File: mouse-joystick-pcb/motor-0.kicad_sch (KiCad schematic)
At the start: 28 parts, among them J1 Conn_01x04_P3.5mm_TBH_Horizon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, J2 Conn_01x02_P3.5mm_TBH_Horizon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, J3 Conn_01x05_P3.5mm_TBH_Horizon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, U1 TMC5130A-TA, U2 MAX6816, U5 Logic_LevelTranslator_LSF0102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, X1 16MHz_3.3V

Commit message: Adjust schmatic
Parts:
- removed C1, C2, C4, C5, C8, C9: 0.1uF_100V, Janelia:C_0402_1005Metric, symbol Janelia:C_0.1uF_100V_0402
- removed C10, C11: 2.2uF_100V, Janelia:C_0805_2012Metric, symbol Janelia:C_2.2uF_100V_0805
- removed C12, C13: 100uF_50V, Janelia:CAP_EEEHAH101UAP, symbol Janelia:CP_100uF_50V_8x10.2mm
- removed C3: 22nF_100V, Janelia:C_0603_1608Metric, symbol Janelia:C_22nF_100V_0603
- removed C6: 0.47uF_35V, Janelia:C_0402_1005Metric, symbol Janelia:C_0.47uF_35V_0402
- removed C7: 47uF_10V, Janelia:C_0805_2012Metric, symbol Janelia:C_47uF_10V_0805
- removed J1: Conn_01x04_P3.5mm_TBH_Horizontal_Screw, Janelia:PhoenixContact_MC_1,5_4-G-3.5_1x04_P3.50mm_Horizontal_Screw, symbol Janelia:Conn_01x04_P3.5mm_TBH_Horizontal_Screw
- removed J2: Conn_01x02_P3.5mm_TBH_Horizontal_Screw, Janelia:PhoenixContact_MC_1,5_2-G-3.5_1x02_P3.50mm_Horizontal_Screw, symbol Janelia:Conn_01x02_P3.5mm_TBH_Horizontal_Screw
- removed R5: 10, Janelia:R_0402_1005Metric, symbol Janelia:R_10_62.5mW_0402
- removed U1: TMC5130A-TA, Janelia:TQFP-48-1EP_7x7mm_P0.5mm_EP5x5mm_ThermalVias, symbol Janelia:TMC5130A-TA
- removed U2: MAX6816, Janelia:SOT192P237X122-4N, symbol Janelia:MAX6816
- removed X1: 16MHz_3.3V, Janelia:OSC_ECS-2520S33-160-FN-TR, symbol Janelia:Oscillator_16MHz_3.3V
- added C501, C502, C504, C505, C509, C510: 0.1uF_100V, Janelia:C_0402_1005Metric, symbol Janelia:C_0.1uF_100V_0402
- added C503: 22nF_100V, Janelia:C_0603_1608Metric, symbol Janelia:C_22nF_100V_0603
- added C506: 0.47uF_35V, Janelia:C_0402_1005Metric, symbol Janelia:C_0.47uF_35V_0402
- added C507: 47uF_10V, Janelia:C_0805_2012Metric, symbol Janelia:C_47uF_10V_0805
- added C512, C513: 2.2uF_100V, Janelia:C_0805_2012Metric, symbol Janelia:C_2.2uF_100V_0805
- added C514, C515: 100uF_50V, Janelia:CAP_EEEHAH101UAP, symbol Janelia:CP_100uF_50V_8x10.2mm
- added J501: Conn_01x02_P3.5mm_TBH_Horizontal_Screw, Janelia:PhoenixContact_MC_1,5_2-G-3.5_1x02_P3.50mm_Horizontal_Screw, symbol Janelia:Conn_01x02_P3.5mm_TBH_Horizontal_Screw
- added J502: Conn_01x04_P3.5mm_TBH_Horizontal_Screw, Janelia:PhoenixContact_MC_1,5_4-G-3.5_1x04_P3.50mm_Horizontal_Screw, symbol Janelia:Conn_01x04_P3.5mm_TBH_Horizontal_Screw
- added R503: 10, Janelia:R_0402_1005Metric, symbol Janelia:R_10_62.5mW_0402
- added U501: MAX6816, Janelia:SOT192P237X122-4N, symbol Janelia:MAX6816
- added U502: TMC5130A-TA, Janelia:TQFP-48-1EP_7x7mm_P0.5mm_EP5x5mm_ThermalVias, symbol Janelia:TMC5130A-TA
- added X501: 16MHz_3.3V, Janelia:OSC_ECS-2520S33-160-FN-TR, symbol Janelia:Oscillator_16MHz_3.3V
- renumbered C23 to C508, C25 to C511, C26 to C516, C24 to C517, J3 to J503, R1 to R501, R2 to R502, R9 to R504, U5 to U503
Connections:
- net +3.3V: now also C501.1, C502.1, C505.1, U501.4 (Vcc), U502.10 (VCC_IO), U502.12 (SPI_MODE), X501.4 (VDD)
- net +5V: now also C506.1, R503.1, U502.34 (VCC), U502.39 (VSA)
- net 5VOUT: now also C507.1, R503.2, U502.33 (5VOUT)
- net BMA1: now also J502.4 (Pin_4), U502.46 (OA1)
- net BMA2: now also J502.3 (Pin_3), U502.42 (OA2)
- net BMB1: now also J502.2 (Pin_2), U502.15 (OB1)
- net BMB2: now also J502.1 (Pin_1), U502.19 (OB2)
- net BRA: now also U502.44 (BRA)
- net BRB: now also U502.17 (BRB)
- net CIPO: now also U502.7 (SDO_NAO_CFG0)
- net CLOCK: now also U502.2 (CLK), X501.3 (OUT)
- net COPI: now also U502.5 (SDI_NAI_CFG1)
- net CPI: now also C503.2, U502.37 (CPI)
- net CPO: now also C503.1, U502.35 (CP0)
- net ENABLE: now also U502.29 (~{DRV_EN}_CFG6)
- net ENC_A_LS: now also U502.25 (ENCA_DCIN_CFG5)
- net ENC_B_LS: now also U502.24 (ENCB_DCEN_CFG4)
- net GND: now also C501.2, C502.2, C505.2, C506.2, C507.2, C509.2, C510.2, C512.2, C513.2, C514.2, C515.2, J501.1 (Pin_1), U501.1 (GND), U502.1 (TST_MODE), U502.11 (SD_MODE), U502.13 (GNDP), U502.23 (ENCN_DCO), U502.30 (AIN_IREF), U502.31 (NC), U502.32 (GNDA), U502.36 (NC), U502.48 (GNDP), U502.49 (EP), U502.6 (NC), U502.9 (REFR_DIR), X501.2 (GND)
- net REFL: now also J501.2 (Pin_2), U501.2 (IN)
- net REFL_DEBOUNCED: now also U501.3 (OUT), U502.8 (REFL_STEP)
- net SCK: now also U502.4 (SCK_CFG2)
- net VCP: now also C504.2, U502.38 (VCP)
- net VM: now also C504.1, C509.1, C510.1, C512.1, C513.1, C514.1, C515.1, U502.21 (VS), U502.40 (VS)
- net ~{CS}: now also U502.3 (~{CS}_CFG3)

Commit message: Finish v1.0 schematic
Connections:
- net ENABLE is gone; now on net GND: U502.29 (~{DRV_EN}_CFG6)
- net DIAG0: now reaches U502.26 (SWN_DIAG0)
- net +3.3V renamed VIO
- no-connect marks 5 -> 4
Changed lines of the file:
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@@
   (title_block
     (title "mouse-joystick-pcb")
-    (date "2024-10-07")
+    (date "2024-10-08")
     (rev "1.0")
     (company "Peter Polidoro")
@@
   (no_connect (at 270.51 139.7))
   (no_connect (at 85.09 44.45))
-  (no_connect (at 36.83 121.92))
   (no_connect (at 36.83 124.46))
   (no_connect (at 36.83 127))
@@
     (stroke (width 0) (type default))
   )
+  (wire (pts (xy 36.83 121.92) (xy 34.29 121.92))
+    (stroke (width 0) (type default))
+  )
   (wire (pts (xy 36.83 134.62) (xy 34.29 134.62))
     (stroke (width 0) (type default))
@@
     (effects (font (size 1.27 1.27)) (justify left bottom))
   )
+  (label "GND" (at 34.29 116.84 180) (fields_autoplaced)
+    (effects (font (size 1.27 1.27)) (justify right bottom))
+  )
   (label "VM" (at 135.89 36.83 90) (fields_autoplaced)
     (effects (font (size 1.27 1.27)) (justify left bottom))
@@
     (effects (font (size 1.27 1.27)) (justify left bottom))
   )
-  (hierarchical_label "+3.3V" (shape passive) (at 53.34 39.37 180) (fields_autoplaced)
+  (hierarchical_label "VIO" (shape passive) (at 53.34 39.37 180) (fields_autoplaced)
     (effects (font (size 1.27 1.27)) (justify right))
   )
@@
     (effects (font (size 1.27 1.27)) (justify right))
   )
-  (hierarchical_label "ENABLE" (shape input) (at 34.29 116.84 180) (fields_autoplaced)
-    (effects (font (size 1.27 1.27)) (justify right))
-  )
   (hierarchical_label "CIPO" (shape output) (at 34.29 93.98 180) (fields_autoplaced)
     (effects (font (size 1.27 1.27)) (justify right))
   )
+  (hierarchical_label "DIAG0" (shape output) (at 34.29 121.92 180) (fields_autoplaced)
+    (effects (font (size 1.27 1.27)) (justify right))
+  )

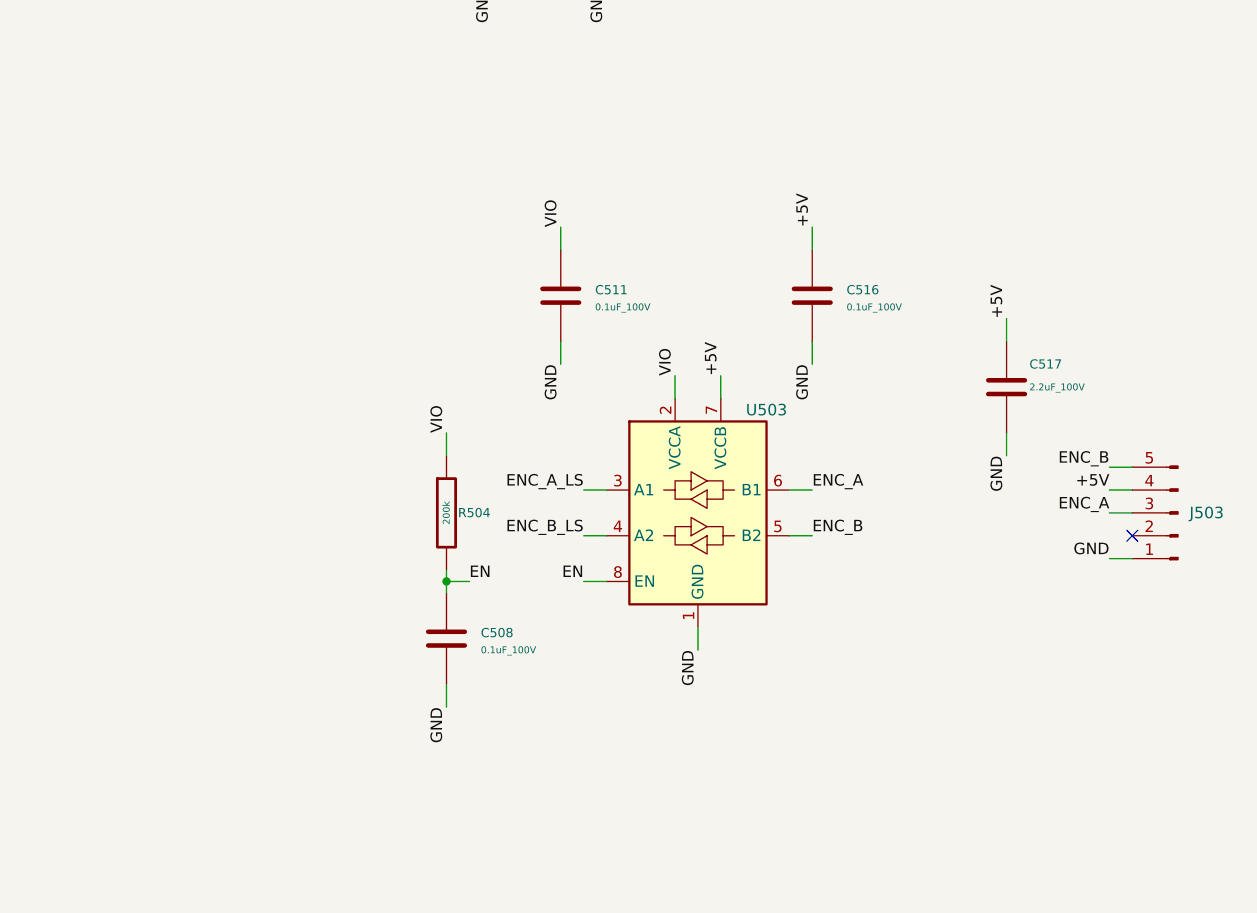
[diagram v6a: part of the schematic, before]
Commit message: Change encoder connector
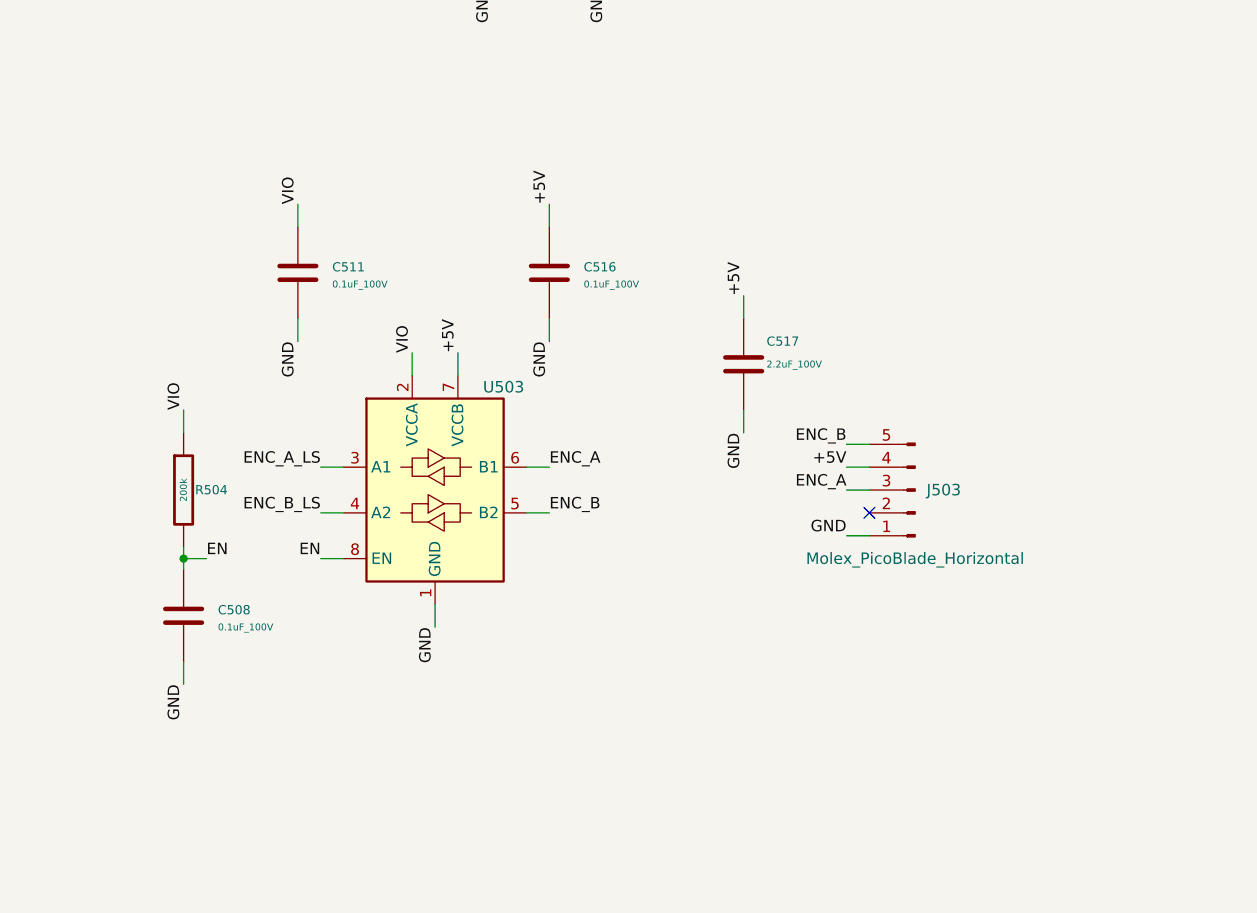
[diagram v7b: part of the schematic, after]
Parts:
- removed J503: Conn_01x05_P3.5mm_TBH_Horizontal_Screw, Janelia:PhoenixContact_MC_1,5_5-G-3.5_1x05_P3.50mm_Horizontal_Screw, symbol Janelia:Conn_01x05_P3.5mm_TBH_Horizontal_Screw
- added J503: Molex_PicoBlade_Horizontal, Janelia:MOLEX_0532610571, symbol Janelia:Conn_01x05_P1.25mm_Molex_PicoBlade_Horizontal
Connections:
- net +5V: now also J503.4 (Pin_4)
- net ENC_A: now also J503.3 (Pin_3)
- net ENC_B: now also J503.5 (Pin_5)
- net GND: now also J503.1 (Pin_1)
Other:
- moved on the sheet: C508, C511, C516, C517, R504, U503

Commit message: Finish routing
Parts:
- added R505: 1.8k, Janelia:R_0402_1005Metric, symbol Janelia:R_1.8k_0402
- C507: LCSC C2182652 -> C6119904; Manufacturer TDK Corporation -> HRE; Manufacturer Part Number C2012X5R1A476M125AC -> CGA0805X5R476M100MT; Vendor Digi-Key -> JLCPCB; Vendor Part Number 445-8239-1-ND -> C6119904
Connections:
- net VIO: now also R505.1
- net ~{CS}: now also R505.2
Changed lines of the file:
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@@
   (title_block
     (title "mouse-joystick-pcb")
-    (date "2024-10-15")
+    (date "2024-10-23")
     (rev "1.0")
     (company "Peter Polidoro")
@@
     (stroke (width 0) (type default))
   )
+  (wire (pts (xy 95.25 72.39) (xy 95.25 69.85))
+    (stroke (width 0) (type default))
+  )
   (wire (pts (xy 74.93 119.38) (xy 72.39 119.38))
     (stroke (width 0) (type default))
@@
     (stroke (width 0) (type default))
   )
+  (wire (pts (xy 53.34 44.45) (xy 55.88 44.45))
+    (stroke (width 0) (type default))
+  )
   (wire (pts (xy 43.18 177.8) (xy 40.64 177.8))
     (stroke (width 0) (type default))
@@
     (stroke (width 0) (type default))
   )
+  (wire (pts (xy 95.25 85.09) (xy 95.25 87.63))
+    (stroke (width 0) (type default))
+  )
   (wire (pts (xy 53.34 36.83) (xy 55.88 36.83))
     (stroke (width 0) (type default))
@@
     (effects (font (size 1.27 1.27)) (justify left bottom))
   )
+  (label "VIO" (at 95.25 69.85 90) (fields_autoplaced)
+    (effects (font (size 1.27 1.27)) (justify left bottom))
+  )
   (label "VM" (at 212.09 63.5 90) (fields_autoplaced)
     (effects (font (size 1.27 1.27)) (justify left bottom))
@@
     (effects (font (size 1.27 1.27)) (justify left bottom))
   )
+  (label "~{CS}" (at 34.29 86.36 180) (fields_autoplaced)
+    (effects (font (size 1.27 1.27)) (justify right bottom))
+  )
   (label "VM" (at 212.09 36.83 90) (fields_autoplaced)
     (effects (font (size 1.27 1.27)) (justify left bottom))
   )
+  (label "~{CS}" (at 95.25 87.63 270) (fields_autoplaced)
+    (effects (font (size 1.27 1.27)) (justify right bottom))
+  )
   (label "CPO" (at 123.19 36.83 90) (fields_autoplaced)
     (effects (font (size 1.27 1.27)) (justify left bottom))
@@
   (label "CPO" (at 34.29 76.2 180) (fields_autoplaced)
     (effects (font (size 1.27 1.27)) (justify right bottom))
+  )
+  (label "~{CS}" (at 55.88 44.45 0) (fields_autoplaced)
+    (effects (font (size 1.27 1.27)) (justify left bottom))
   )
   (label "VM" (at 224.79 39.37 90) (fields_autoplaced)
@@
     (effects (font (size 1.27 1.27)) (justify right))
   )
-  (hierarchical_label "~{CS}" (shape input) (at 34.29 86.36 180) (fields_autoplaced)
+  (hierarchical_label "~{CS}" (shape input) (at 53.34 44.45 180) (fields_autoplaced)
     (effects (font (size 1.27 1.27)) (justify right))
   )
@@
       (effects (font (size 1.524 1.524)))
     )
-    (property "Vendor" "Digi-Key" (at 189.23 39.37 0)
-      (effects (font (size 1.524 1.524)) hide)
-    )
-    (property "Vendor Part Number" "445-8239-1-ND" (at 191.77 36.83 0)
+    (property "Vendor" "JLCPCB" (at 189.23 39.37 0)
+      (effects (font (size 1.524 1.524)) hide)
+    )
+    (property "Vendor Part Number" "C6119904" (at 191.77 36.83 0)
       (effects (font (size 1.524 1.524)) hide)
     )
@@
       (effects (font (size 1.27 1.27)) hide)
     )
-    (property "Manufacturer" "TDK Corporation" (at 186.69 44.45 0)
-      (effects (font (size 1.27 1.27)) hide)
-    )
-    (property "Manufacturer Part Number" "C2012X5R1A476M125AC" (at 186.69 44.45 0)
+    (property "Manufacturer" "HRE" (at 186.69 44.45 0)
+      (effects (font (size 1.27 1.27)) hide)
+    )
+    (property "Manufacturer Part Number" "CGA0805X5R476M100MT" (at 186.69 44.45 0)
       (effects (font (size 1.27 1.27)) hide)
     )
@@
       (effects (font (size 1.524 1.524)) hide)
     )
-    (property "LCSC" "C2182652" (at 186.69 44.45 0)
+    (property "LCSC" "C6119904" (at 186.69 44.45 0)
       (effects (font (size 1.27 1.27)) hide)
     )
@@
         )
       )
+    )
+  )
+  (symbol (lib_id "Janelia:R_1.8k_0402") (at 95.25 78.74 0) (unit 1)
+    (in_bom yes) (on_board yes) (dnp no)
+    (property "Reference" "R505" (at 96.52 78.74 0)
+      (effects (font (size 1.016 1.016)) (justify left))
+    )
+    (property "Value" "1.8k" (at 95.25 78.74 90) (do_not_autoplace)
+      (effects (font (size 0.762 0.762)))
+    )
+    (property "Footprint" "Janelia:R_0402_1005Metric" (at 93.472 78.74 90)
+      (effects (font (size 0.762 0.762)) hide)
+    )
+    (property "Datasheet" "" (at 97.282 78.74 90)
+      (effects (font (size 0.762 0.762)))
+    )
+    (property "Vendor" "JLCPCB" (at 99.822 76.2 90)
+      (effects (font (size 1.524 1.524)) hide)
+    )
+    (property "Vendor Part Number" "C409855" (at 102.362 73.66 90)
+      (effects (font (size 1.524 1.524)) hide)
+    )
+    (property "Synopsis" "RES SMD 1.8K OHM 5% 100mW" (at 104.902 71.12 90)
+      (effects (font (size 1.524 1.524)) hide)
+    )
+    (property "Package" "0402" (at 95.25 78.74 0)
+      (effects (font (size 1.27 1.27)) hide)
+    )
+    (property "Manufacturer" "PANASONIC" (at 95.25 78.74 0)
+      (effects (font (size 1.27 1.27)) hide)
+    )
+    (property "Manufacturer Part Number" "ERJ2GEJ182X" (at 95.25 78.74 0)
+      (effects (font (size 1.27 1.27)) hide)
+    )
+    (property "LCSC" "C409855" (at 95.25 78.74 0)
+      (effects (font (size 1.27 1.27)) hide)
+    )
+    (pin "2")
+    (pin "1")
+    (instances
+      (project "mouse-joystick-pcb"
+        (path "/df2b2e89-e055-4140-95de-f1df723db034/843743ad-cb97-4017-b3d5-10e69a46da88"
+          (reference "R505") (unit 1)
+        )
+      )
